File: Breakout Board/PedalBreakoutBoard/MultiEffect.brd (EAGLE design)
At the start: 65.7 x 61 mm, 52 parts, among them IC1 LD1117V, IC2 MCP6004P, U1 OPA1652AID

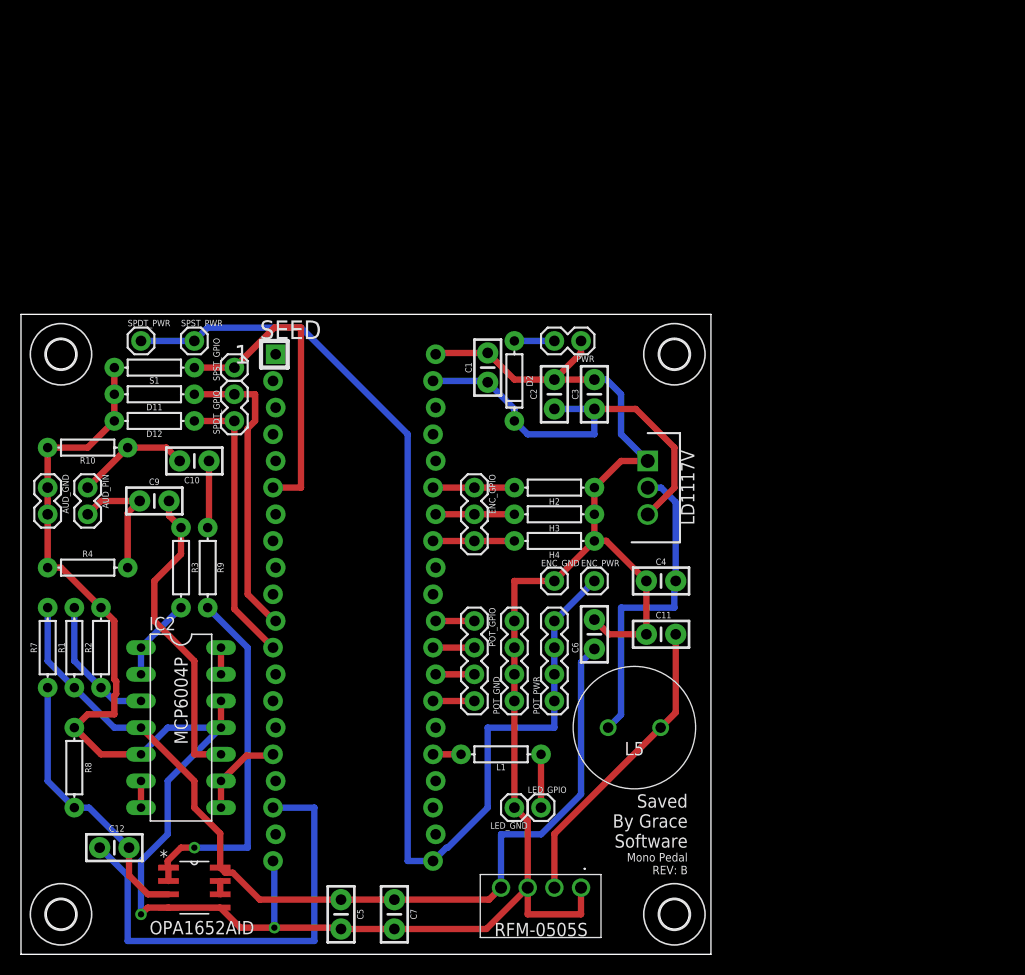
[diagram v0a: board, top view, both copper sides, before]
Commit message: DP-6 - Add connections for OLED
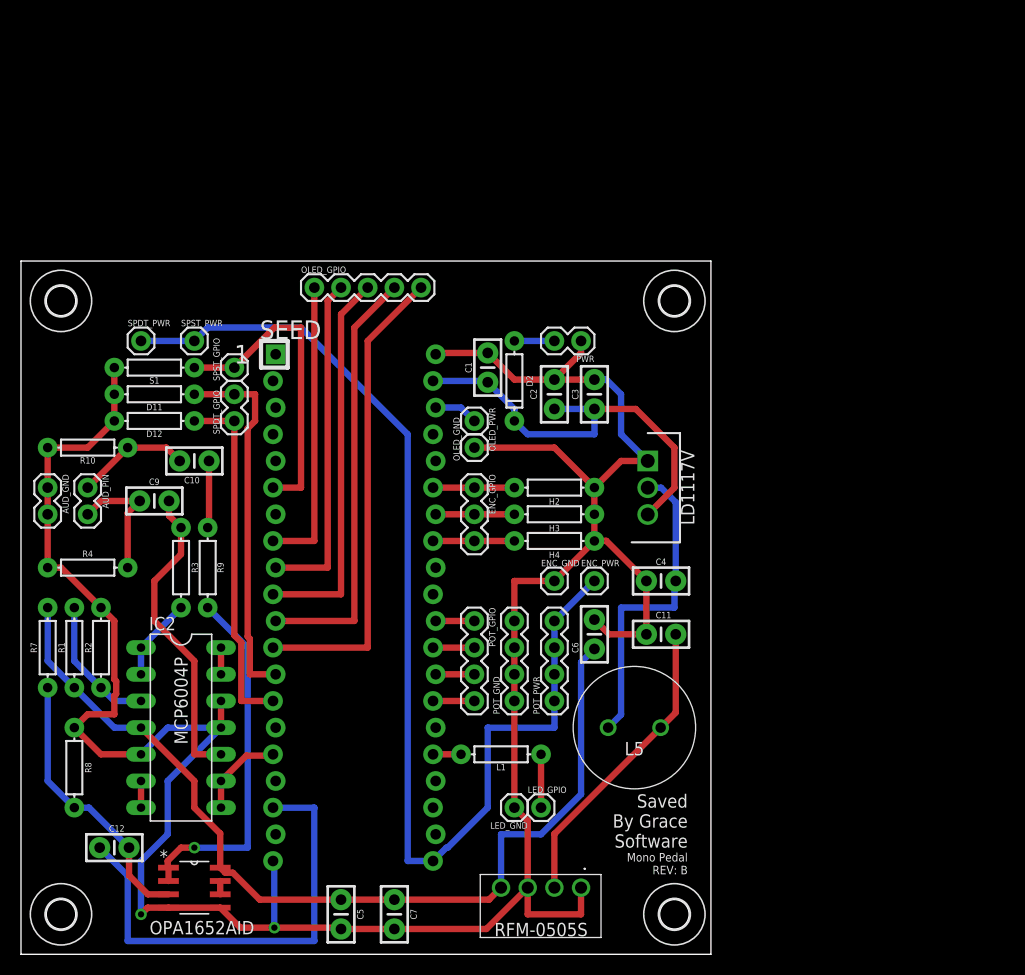
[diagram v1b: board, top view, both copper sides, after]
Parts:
- added OLED_GND, OLED_PWR: (no value), SparkFun-Connectors:1X01
- added OLED_GPIO: (no value), SparkFun-Connectors:1X05
- moved H6 5.08 mm to (62.2, 62.2)
- moved H8 5.08 mm to (3.81, 62.2)
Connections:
- new net +3V3_D: OLED_PWR.1, SEED.38
- new net CS: OLED_GPIO.1, SEED.8
- new net DC: OLED_GPIO.3, SEED.10
- new net RES: OLED_GPIO.5, SEED.12
- new net SCL: OLED_GPIO.2, SEED.9
- new net SDA: OLED_GPIO.4, SEED.11
- net GND: now also OLED_GND.1
- net SPDT1_1: now also SEED.13; no longer SEED.11
- net SPDT1_2: now also SEED.14; no longer SEED.12
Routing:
- net RES: track 0.00 -> 45.4 mm
- net SDA: track 0.00 -> 40.8 mm
- net DC: track 0.00 -> 36.7 mm
- net SCL: track 0.00 -> 32.1 mm
- net CS: track 0.00 -> 28.1 mm
- net GND: track 240.2 -> 253.2 mm
- net SPDT1_2: track 26.9 -> 33.8 mm
- net SPDT1_1: track 28.8 -> 35.3 mm
- net +3V3_D: track 0.00 -> 4.21 mm
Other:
- board size 65.7 x 61 mm -> 65.7 x 66 mm
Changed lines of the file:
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@@
 <plain>
 <wire x1="0" y1="0" x2="65.71" y2="0" width="0" layer="20"/>
-<wire x1="65.71" y1="0" x2="65.71" y2="60.95" width="0" layer="20"/>
-<wire x1="65.71" y1="60.95" x2="0" y2="60.95" width="0" layer="20"/>
-<wire x1="0" y1="60.95" x2="0" y2="0" width="0" layer="20"/>
+<wire x1="65.71" y1="0" x2="65.71" y2="66.03" width="0" layer="20"/>
+<wire x1="65.71" y1="66.03" x2="0" y2="66.03" width="0" layer="20"/>
+<wire x1="0" y1="66.03" x2="0" y2="0" width="0" layer="20"/>
 <text x="63.5" y="10.16" size="1.27" layer="25" align="bottom-right">Saved
 By Grace
@@
 <attribute name="POPULARITY" value="15" x="57.15" y="-57.15" size="1.778" layer="27" display="off"/>
 </element>
-<element name="H6" library="holes" library_urn="urn:adsk.eagle:library:237" package="2,8" package3d_urn="urn:adsk.eagle:package:14271/1" value="MOUNT-HOLE2.8" x="62.23" y="57.15" smashed="yes">
-<attribute name="POPULARITY" value="15" x="123.19" y="-3.81" size="1.778" layer="27" display="off"/>
+<element name="H6" library="holes" library_urn="urn:adsk.eagle:library:237" package="2,8" package3d_urn="urn:adsk.eagle:package:14271/1" value="MOUNT-HOLE2.8" x="62.23" y="62.23" smashed="yes">
+<attribute name="POPULARITY" value="15" x="123.19" y="1.27" size="1.778" layer="27" display="off"/>
 </element>
 <element name="H7" library="holes" library_urn="urn:adsk.eagle:library:237" package="2,8" package3d_urn="urn:adsk.eagle:package:14271/1" value="MOUNT-HOLE2.8" x="62.23" y="3.81" smashed="yes">
 <attribute name="POPULARITY" value="15" x="130.81" y="-57.15" size="1.778" layer="27" display="off"/>
 </element>
-<element name="H8" library="holes" library_urn="urn:adsk.eagle:library:237" package="2,8" package3d_urn="urn:adsk.eagle:package:14271/1" value="MOUNT-HOLE2.8" x="3.81" y="57.15" smashed="yes">
-<attribute name="POPULARITY" value="15" x="80.01" y="-3.81" size="1.778" layer="27" display="off"/>
+<element name="H8" library="holes" library_urn="urn:adsk.eagle:library:237" package="2,8" package3d_urn="urn:adsk.eagle:package:14271/1" value="MOUNT-HOLE2.8" x="3.81" y="62.23" smashed="yes">
+<attribute name="POPULARITY" value="15" x="80.01" y="1.27" size="1.778" layer="27" display="off"/>
 </element>
 <element name="ENC_PWR" library="SparkFun-Connectors" library_urn="urn:adsk.eagle:library:513" package="1X01" package3d_urn="urn:adsk.eagle:package:38028/1" value="" x="54.61" y="35.56" smashed="yes">
@@
 <attribute name="NAME" x="44.577" y="45.72" size="0.6096" layer="25" font="vector" ratio="20" rot="R270"/>
 <attribute name="VALUE" x="41.148" y="45.72" size="0.6096" layer="27" font="vector" ratio="20" rot="R270"/>
+</element>
+<element name="OLED_GPIO" library="SparkFun-Connectors" library_urn="urn:adsk.eagle:library:513" package="1X05" package3d_urn="urn:adsk.eagle:package:38104/1" value="" x="27.94" y="63.5" smashed="yes">
+<attribute name="NAME" x="26.67" y="64.897" size="0.6096" layer="25" font="vector" ratio="20"/>
+<attribute name="VALUE" x="26.67" y="61.468" size="0.6096" layer="27" font="vector" ratio="20"/>
+</element>
+<element name="OLED_PWR" library="SparkFun-Connectors" library_urn="urn:adsk.eagle:library:513" package="1X01" package3d_urn="urn:adsk.eagle:package:38028/1" value="" x="43.18" y="50.8" smashed="yes" rot="R270">
+<attribute name="NAME" x="44.577" y="52.07" size="0.6096" layer="25" font="vector" ratio="20" rot="R270"/>
+<attribute name="VALUE" x="41.656" y="52.07" size="0.6096" layer="27" font="vector" ratio="20" rot="R270" align="top-left"/>
+</element>
+<element name="OLED_GND" library="SparkFun-Connectors" library_urn="urn:adsk.eagle:library:513" package="1X01" package3d_urn="urn:adsk.eagle:package:38028/1" value="" x="43.18" y="48.26" smashed="yes" rot="R90">
+<attribute name="NAME" x="41.783" y="46.99" size="0.6096" layer="25" font="vector" ratio="20" rot="R90"/>
+<attribute name="VALUE" x="44.704" y="46.99" size="0.6096" layer="27" font="vector" ratio="20" rot="R90" align="top-left"/>
 </element>
 </elements>
@@
 <wire x1="57.15" y1="46.99" x2="59.69" y2="46.99" width="0.6096" layer="1"/>
 <wire x1="57.15" y1="49.53" x2="59.69" y2="46.99" width="0.6096" layer="16"/>
+<contactref element="OLED_GND" pad="1"/>
+<wire x1="43.18" y1="48.26" x2="50.8" y2="48.26" width="0.6096" layer="1"/>
+<wire x1="50.8" y1="48.26" x2="54.61" y2="44.45" width="0.6096" layer="1"/>
 </signal>
 <signal name="SPST1">
@@
 </signal>
 <signal name="SPDT1_1">
-<contactref element="SEED" pad="11"/>
 <contactref element="D11" pad="P$2"/>
 <contactref element="SPDT_GPIO" pad="2"/>
@@
 <wire x1="22.2956625" y1="53.34" x2="22.2956625" y2="50.8" width="0.6096" layer="1"/>
 <wire x1="22.2956625" y1="50.8" x2="21.59" y2="50.0943375" width="0.6096" layer="1"/>
-<wire x1="21.59" y1="34.29" x2="24.13" y2="31.75" width="0.6096" layer="1"/>
-<wire x1="24.13" y1="31.75" x2="24.257" y2="31.75" width="0.6096" layer="1"/>
-<wire x1="21.59" y1="50.0943375" x2="21.59" y2="34.29" width="0.6096" layer="1"/>
+<contactref element="SEED" pad="13"/>
+<wire x1="21.59" y1="30.2548875" x2="21.7932" y2="30.0516875" width="0.6096" layer="1"/>
+<wire x1="21.7932" y1="30.0516875" x2="21.7932" y2="26.67" width="0.6096" layer="1"/>
+<wire x1="21.7932" y1="26.67" x2="24.257" y2="26.67" width="0.6096" layer="1"/>
+<wire x1="21.59" y1="50.0943375" x2="21.59" y2="30.2548875" width="0.6096" layer="1"/>
 </signal>
 <signal name="SPDT1_2">
-<contactref element="SEED" pad="12"/>
 <contactref element="D12" pad="P$2"/>
 <contactref element="SPDT_GPIO" pad="1"/>
 <wire x1="16.51" y1="50.8" x2="20.32" y2="50.8" width="0.6096" layer="1"/>
-<wire x1="20.32" y1="32.893" x2="24.003" y2="29.21" width="0.6096" layer="1"/>
-<wire x1="20.32" y1="50.8" x2="20.32" y2="32.893" width="0.6096" layer="1"/>
+<contactref element="SEED" pad="14"/>
+<wire x1="20.32" y1="30.3754125" x2="20.9804" y2="29.7150125" width="0.6096" layer="1"/>
+<wire x1="20.9804" y1="29.7150125" x2="20.9804" y2="24.13" width="0.6096" layer="1"/>
+<wire x1="20.9804" y1="24.13" x2="24.003" y2="24.13" width="0.6096" layer="1"/>
+<wire x1="20.32" y1="50.8" x2="20.32" y2="30.3754125" width="0.6096" layer="1"/>
 </signal>
 <signal name="N$2">
@@
 <wire x1="2.54" y1="33.02" x2="2.54" y2="27.94" width="0.6096" layer="16"/>
 <contactref element="C5" pad="1"/>
-<wire x1="22.74021875" y1="5.207" x2="30.48" y2="5.207" width="0.6096" layer="1"/>
-<wire x1="30.48" y1="5.207" x2="30.5435" y2="5.1435" width="0.6096" layer="1"/>
 <contactref element="C7" pad="1"/>
-<wire x1="30.48" y1="5.207" x2="35.56" y2="5.207" width="0.6096" layer="1"/>
 <wire x1="35.56" y1="5.207" x2="44.577" y2="5.207" width="0.6096" layer="1"/>
 <wire x1="44.577" y1="5.207" x2="45.72" y2="6.35" width="0.6096" layer="1"/>
 <contactref element="C6" pad="1"/>
 <wire x1="53.34" y1="27.813" x2="54.61" y2="29.083" width="0.6096" layer="16"/>
+<wire x1="22.74021875" y1="5.207" x2="30.48" y2="5.207" width="0.6096" layer="1"/>
+<wire x1="30.48" y1="5.207" x2="35.56" y2="5.207" width="0.6096" layer="1"/>
 </signal>
 <signal name="N$6">
@@
 <wire x1="49.53" y1="19.05" x2="49.53" y2="13.97" width="0.6096" layer="1"/>
 </signal>
+<signal name="+3V3_D">
+<contactref element="OLED_PWR" pad="1"/>
+<contactref element="SEED" pad="38"/>
+<wire x1="39.497" y1="52.07" x2="41.91" y2="52.07" width="0.6096" layer="16"/>
+<wire x1="41.91" y1="52.07" x2="43.18" y2="50.8" width="0.6096" layer="16"/>
+</signal>
+<signal name="SCL">
+<contactref element="SEED" pad="9"/>
+<wire x1="24.257" y1="36.83" x2="29.21" y2="36.83" width="0.6096" layer="1"/>
+<contactref element="OLED_GPIO" pad="2"/>
+<wire x1="29.21" y1="62.23" x2="30.48" y2="63.5" width="0.6096" layer="1"/>
+<wire x1="29.21" y1="36.83" x2="29.21" y2="62.23" width="0.6096" layer="1"/>
+</signal>
+<signal name="SDA">
+<contactref element="SEED" pad="11"/>
+<wire x1="24.257" y1="31.75" x2="31.75" y2="31.75" width="0.6096" layer="1"/>
+<contactref element="OLED_GPIO" pad="4"/>
+<wire x1="31.75" y1="59.69" x2="35.56" y2="63.5" width="0.6096" layer="1"/>
+<wire x1="31.75" y1="31.75" x2="31.75" y2="59.69" width="0.6096" layer="1"/>
+</signal>
+<signal name="RES">
+<contactref element="SEED" pad="12"/>
+<wire x1="24.003" y1="29.21" x2="33.02" y2="29.21" width="0.6096" layer="1"/>
+<contactref element="OLED_GPIO" pad="5"/>
+<wire x1="33.02" y1="58.42" x2="38.1" y2="63.5" width="0.6096" layer="1"/>
+<wire x1="33.02" y1="29.21" x2="33.02" y2="58.42" width="0.6096" layer="1"/>
+</signal>
+<signal name="DC">
+<contactref element="SEED" pad="10"/>
+<wire x1="24.003" y1="34.29" x2="30.48" y2="34.29" width="0.6096" layer="1"/>
+<contactref element="OLED_GPIO" pad="3"/>
+<wire x1="30.48" y1="60.96" x2="33.02" y2="63.5" width="0.6096" layer="1"/>
+<wire x1="30.48" y1="34.29" x2="30.48" y2="60.96" width="0.6096" layer="1"/>
+</signal>
+<signal name="CS">
+<contactref element="OLED_GPIO" pad="1"/>
+<contactref element="SEED" pad="8"/>
+<wire x1="24.003" y1="39.37" x2="27.94" y2="39.37" width="0.6096" layer="1"/>
+<wire x1="27.94" y1="39.37" x2="27.94" y2="63.5" width="0.6096" layer="1"/>
+</signal>
 </signals>

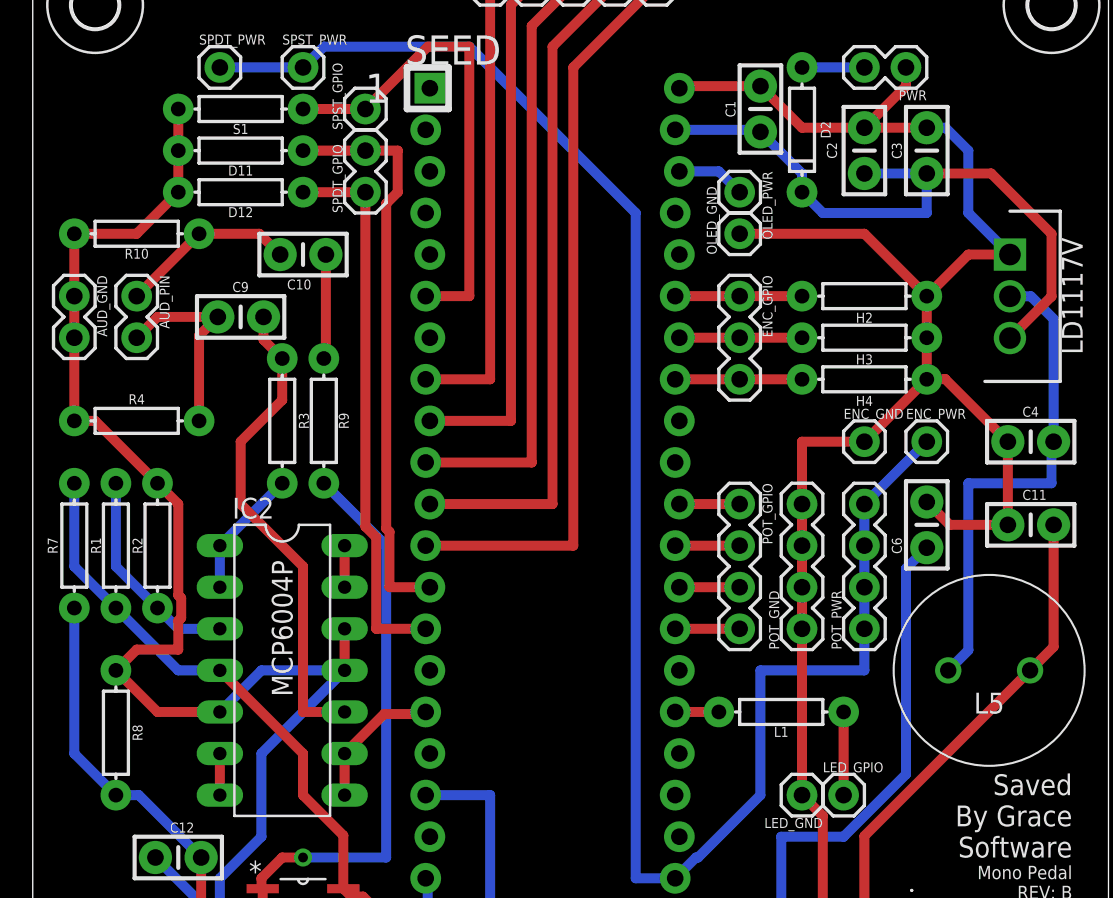
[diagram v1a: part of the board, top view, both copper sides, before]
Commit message: DP-6 - Add additional POT for output volume
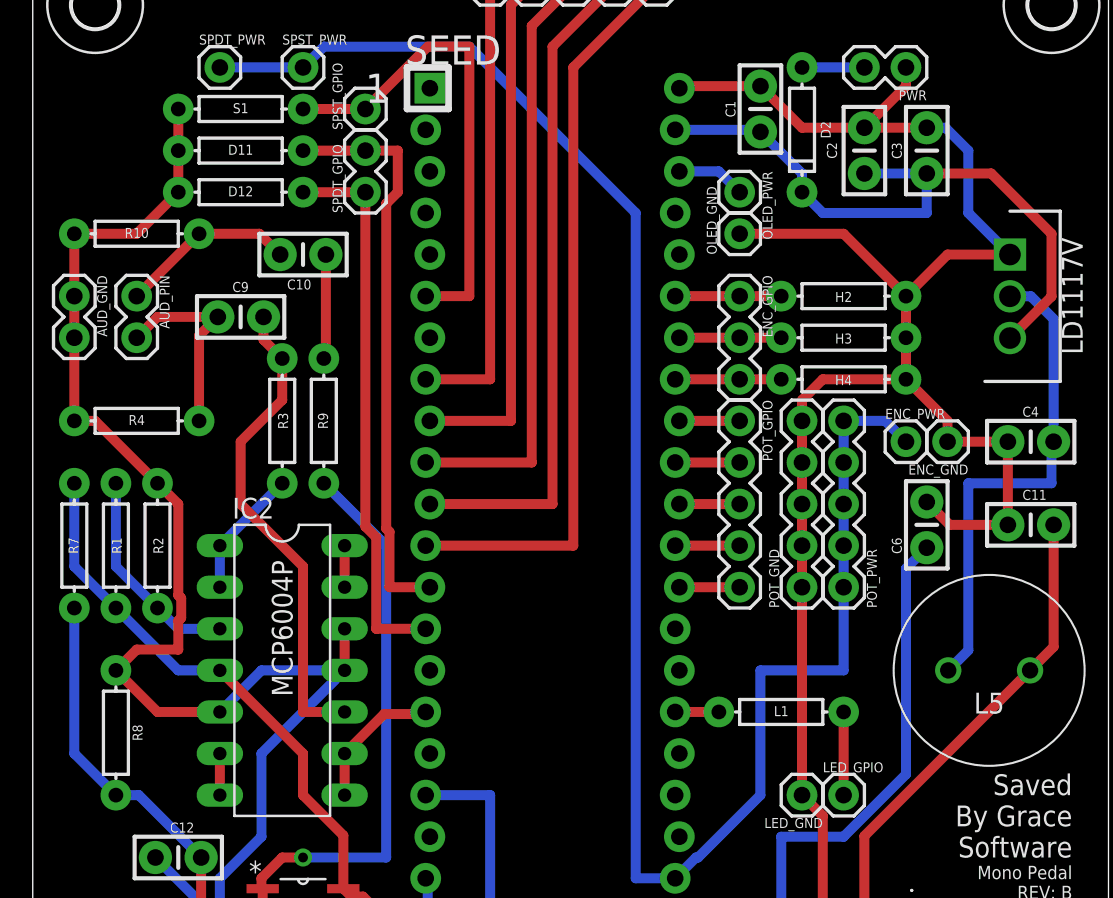
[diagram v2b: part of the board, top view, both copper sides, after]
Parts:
- POT_GND, POT_GPIO, POT_PWR: device SparkFun-Connectors:1X04 -> SparkFun-Connectors:1X05
- moved ENC_GND 5.08 mm to (55.9, 35.6), turned to 180 degrees
- moved POT_GPIO 5.08 mm to (43.2, 36.8)
- moved POT_PWR 2.84 mm to (49.5, 26.7)
- moved POT_GND 2.54 mm to (47.0, 26.7)
- moved ENC_PWR 1.27 mm to (53.3, 35.6)
- moved H2 1.27 mm to (49.5, 44.5)
- moved H3 1.27 mm to (49.5, 41.9)
- moved H4 1.27 mm to (49.5, 39.4)
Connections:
- new net POT5: POT_GPIO.5, SEED.28
- net +3V3_A: now also POT_PWR.5
- net GND: now also POT_GND.5
- net POT1: now also SEED.32; no longer SEED.30
- net POT2: now also SEED.31; no longer SEED.29
- net POT3: now also SEED.30; no longer SEED.28
- net POT4: now also SEED.29; no longer SEED.27
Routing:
- net POT5: track 0.00 -> 3.68 mm
- net +3V3_A: track 110.0 -> 112.8 mm
- net GND: track 253.2 -> 255.4 mm
- net ENC_SW: track 7.75 -> 6.48 mm
- net ENC_B: track 7.49 -> 6.22 mm
- net ENC_A: track 7.75 -> 6.48 mm
